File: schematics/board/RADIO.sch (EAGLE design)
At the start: 50 parts, among them J1 IPX-RADIO, J2 IPX-ANT

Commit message: Платки там
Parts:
- removed C1: 100nF, rcl:C-EUC0603
- removed C2: 220uF, UNKNOWN-2024:ECAPECAP220
- removed J1: IPX-RADIO, UNKNOWN-2024:U.FL-R-SMT-1_10_
- removed J2: IPX-ANT, UNKNOWN-2024:U.FL-R-SMT-1_10_
- removed LED1: AMP1, led:LEDCHIPLED_0603
- removed LED2: AMP2, led:LEDCHIPLED_0603
- removed NRF24LO1: NRF24L01_ML01SP4, UNKNOWN-2024:NRF24L01_ML01SP4
- removed R1, R2, R3, R4: 2k, rcl:R-US_R0603
- removed ROTATE1, ROTATE2, SW: CONNECT_3, UNKNOWN-2024:CONNECT_3
- removed XQ-02A: XQ-02A, UNKNOWN-2024:XQ-02A
- added JP1: (no value), pinhead:PINHD-1X10
- added JP2: (no value), pinhead:PINHD-1X16
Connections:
- removed net ANT_RADIO: J2.3, XQ-02A.ANT
- removed net N$1: LED1.C, R1.2
- removed net N$2: LED2.C, R2.2
- removed net N$3: LED1.A, ROTATE1.PIN
- removed net N$4: LED2.A, ROTATE2.PIN
- removed net N$5: R2.1, XQ-02A.LED2
- removed net N$6: R1.1, XQ-02A.LED1
- removed net N$7: R3.2, SW.P$1
- removed net N$8: R4.2, SW.P$3
- removed net RF-IN: J1.3, XQ-02A.RF-IN
- removed net SW: SW.PIN, XQ-02A.SW
- net 3V3: no longer NRF24LO1.VCC, ROTATE1.P$1, ROTATE2.P$1
- net 5V: no longer C1.2, C2.1, R3.1, XQ-02A.5V
- net CE_RADIO: no longer NRF24LO1.CE
- net CS_RADIO: no longer NRF24LO1.CSN
- net GND: no longer C1.1, C2.2, J1.1, J1.2, J2.1, J2.2, NRF24LO1.GND, R4.1, ROTATE1.P$3, ROTATE2.P$3, XQ-02A.GND
- net IRQ_RADIO: no longer NRF24LO1.IRQ
- net MISO_RADIO: no longer NRF24LO1.MISO
- net MOSI_RADIO: no longer NRF24LO1.MOSI
- net SCK_RADIO: no longer NRF24LO1.SCK

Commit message: ПЛАТЫ, АААААААААААААААААААААААААААА
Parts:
- added JP3: (no value), pinhead:PINHD-1X18
- added R1: 10k, rcl:R-US_R0603
- added R2: 100R, rcl:R-US_R0603
- added S1: (no value), UNKNOWN-2024:UNICS-SWITCHSS_12D11
- added SI2302CDS: SI2302CDS, CanCubeSat:SI2302CDS
- added U$10: LIS3MDL, UNKNOWN-2024:LIS3MDL
- added U$18: MOLEX-2-1.25, UNKNOWN-2024:MOLEX-2-1.25
- added U$4: E220-400T22S, UNKNOWN-2024:E220-400T22S
- added U$9: LSM6DS3_WITHOUT, UNKNOWN-2024:LSM6DS3_WITHOUT
- added X2: AKKUM, UNKNOWN-2024:JST-2-2.5
- JP2: device pinhead:PINHD-1X16 -> pinhead:PINHD-1X8
- U$6: value PBS_SMD_X13 -> MOLEX-2-1.25; device UNKNOWN-2024:PBS_SMD_X13 -> UNKNOWN-2024:MOLEX-2-1.25
- U$7: value PBS_SMD_X9 -> MOLEX-2-1.25; device UNKNOWN-2024:PBS_SMD_X9 -> UNKNOWN-2024:MOLEX-2-1.25
- U$8: value PBS_SMD_X13 -> JST-6-2.5; device UNKNOWN-2024:PBS_SMD_X13 -> UNKNOWN-2024:JST-6-2.5
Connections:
- removed net ADC_FOTO: U$6.10, U$8.4
- removed net CE_RADIO: U$7.1
- removed net CS_RADIO: U$7.2
- removed net DIR_DRIVER: U$6.2, U$8.12
- removed net IRQ_RADIO: U$7.3
- removed net LATCH_SR: U$6.5, U$8.9
- removed net MISO_RADIO: U$7.5
- removed net MOSI_RADIO: U$7.4
- removed net OE_SR: U$6.6, U$8.8
- removed net RX1_BLE: U$6.4, U$8.10
- removed net RX2_GPS: GPS-NEO7M.TX, U$7.8
- removed net SCK_RADIO: U$7.6
- removed net STEP_DRIVER: U$6.1, U$8.13
- removed net TX1_BLE: U$6.3, U$8.11
- removed net TX2_GPS: GPS-NEO7M.RX, U$7.7
- new net 3V7: JP1.10
- new net AUX_RADIO: JP3.10, U$4.AUX
- new net BUS+_OUT: S1.S, X2.1
- new net C0: JP2.1, JP3.1
- new net CS_LIS: JP1.8, U$10.CS
- new net CS_LSM: JP1.9, U$9.CS
- new net GERMO: JP3.18, R2.1
- new net LATCH: JP1.5, U$8.1
- new net M0_RADIO: JP3.12, U$4.M0
- new net M1_RADIO: JP3.11, U$4.M1
- new net MICS: JP2.4, JP3.4
- new net MISO_SENS: JP1.2
- new net MOSI: U$8.3
- new net MOSI_SENS: JP1.1
- new net N$2: R1.1, R2.2, SI2302CDS.G
- new net N$5: SI2302CDS.D, U$18.1, U$6.1, U$7.1
- new net NH3: JP2.3, JP3.3
- new net NO2: JP2.2, JP3.2
- new net OE: JP1.4, U$8.P$1
- new net RX_GPS: GPS-NEO7M.TX, JP3.14
- new net RX_LIDAR: JP3.15
- new net RX_RADIO: JP1.6, U$4.TXD
- new net SCK: U$8.2
- new net SCK_SENS: JP1.3
- new net SCL: JP2.8, JP3.9
- new net SDA: JP2.7, JP3.8
- new net SHIFT2: U$8.P$2
- new net SHIFT_2: JP3.17
- new net TX_GPS: GPS-NEO7M.RX, JP3.13
- new net TX_LIDAR: JP3.16
- new net TX_RADIO: JP1.7, U$4.RXD
- net 3V3: now also JP3.6, U$10.UCC, U$4.VCC, U$8.4, U$9.3V3; no longer U$6.13, U$8.1
- net 5V: now also JP2.6, JP3.7, U$18.2, U$6.2, U$7.2; no longer U$6.11, U$8.3
- net BUS+: now also S1.P
- net GND: now also JP2.5, JP3.5, R1.2, SI2302CDS.S, U$10.GND, U$4.GND, U$9.GND, X2.2; no longer U$6.12, U$8.2
- net MISO_SR: now also U$10.SDO, U$9.CAO; no longer U$6.8, U$8.6
- net MOSI_SR: now also U$10.SDA, U$9.SDA; no longer U$6.9, U$8.5
- net SCK_SR: now also U$10.SCL, U$9.SCL; no longer U$6.7, U$8.7
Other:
- moved on the sheet: 3V3, 5V, C10, C11, C12, C13, C14, C15, C16, C3, C4, C5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

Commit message: схемы плат
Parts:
- removed U$18, U$6, U$7: MOLEX-2-1.25, UNKNOWN-2024:MOLEX-2-1.25
- added COMPRESS, VALVE1, VALVE2: MOLEX-2-1.25, UNKNOWN-2024:MOLEX-2-1.25
- LSM6DS3: value LSM6DS3_WITHOUT -> LSM6DS3
- renumbered U$4 to RADIO, U$9 to LSM6DS3
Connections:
- net 5V: now also COMPRESS.2, VALVE1.2, VALVE2.2; no longer U$18.2, U$6.2, U$7.2
- net N$5: now also COMPRESS.1, VALVE1.1, VALVE2.1; no longer U$18.1, U$6.1, U$7.1
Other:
- moved on the sheet: 3V3, 5V, C10, C11, C12, C13, C14, C15, C16, C3, C4, C5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

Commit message: подготовлены файлы для зимней сессии
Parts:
- X2: device UNKNOWN-2024:JST-2-2.5 -> UNKNOWN-2024:JST-3-2.5
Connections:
- net LATCH renamed LATCH_SR
- net OE renamed OE_SR
- removed net 3V7: JP1.10
- removed net MISO_SR: LSM6DS3.CAO, U$10.SDO
- removed net MOSI: U$8.3
- removed net MOSI_SR: LSM6DS3.SDA, U$10.SDA
- removed net SCK: U$8.2
- removed net SCK_SR: LSM6DS3.SCL, U$10.SCL
- removed net SHIFT2: U$8.P$2
- removed net SHIFT_2: JP3.17
- new net 4V: JP1.10, X2.3
- new net SHIFT: JP3.17, U$8.P$2
- net MISO_SENS: now also LSM6DS3.CAO, U$10.SDO
- net MOSI_SENS: now also LSM6DS3.SDA, U$10.SDA, U$8.3
- net SCK_SENS: now also LSM6DS3.SCL, U$10.SCL, U$8.2
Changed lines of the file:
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@@
 <part name="U$10" library="UNKNOWN-2024" deviceset="LIS3MDL" device=""/>
 <part name="S1" library="UNKNOWN-2024" deviceset="UNICS-SWITCH" device="SS_12D11"/>
-<part name="X2" library="UNKNOWN-2024" deviceset="JST-2-2.5" device="" value="AKKUM"/>
+<part name="X2" library="UNKNOWN-2024" deviceset="JST-3-2.5" device="" value="AKKUM"/>
 <part name="JP2" library="pinhead" library_urn="urn:adsk.eagle:library:325" deviceset="PINHD-1X8" device="" package3d_urn="urn:adsk.eagle:package:22409/2"/>
 <part name="SI2302CDS" library="CanCubeSat" deviceset="SI2302CDS" device=""/>
@@
 <sheet>
 <plain>
+<wire x1="-76.2" y1="175.26" x2="304.8" y2="175.26" width="0.1524" layer="90"/>
+<wire x1="304.8" y1="175.26" x2="304.8" y2="-27.94" width="0.1524" layer="90"/>
+<wire x1="304.8" y1="-27.94" x2="-76.2" y2="-27.94" width="0.1524" layer="90"/>
+<wire x1="-76.2" y1="-27.94" x2="-76.2" y2="175.26" width="0.1524" layer="90"/>
 </plain>
 <instances>
@@
 <instance part="X2" gate="G$1" x="-15.24" y="127" smashed="yes">
 <attribute name="VALUE" x="-16.51" y="119.38" size="1.778" layer="96"/>
-<attribute name="NAME" x="-16.51" y="130.302" size="1.778" layer="95"/>
+<attribute name="NAME" x="-16.51" y="132.842" size="1.778" layer="95"/>
 </instance>
 <instance part="JP2" gate="A" x="-45.72" y="25.4" smashed="yes">
@@
 <pinref part="LSM6DS3" gate="G$1" pin="GND"/>
 <wire x1="48.26" y1="99.06" x2="58.42" y2="99.06" width="0.1524" layer="91"/>
-<label x="55.88" y="99.06" size="1.778" layer="95"/>
+<label x="53.34" y="99.06" size="1.778" layer="95"/>
 </segment>
 <segment>
 <pinref part="U$10" gate="G$1" pin="GND"/>
-<wire x1="38.1" y1="53.34" x2="25.4" y2="53.34" width="0.1524" layer="91"/>
-<label x="25.4" y="53.34" size="1.778" layer="95"/>
+<wire x1="38.1" y1="53.34" x2="22.86" y2="53.34" width="0.1524" layer="91"/>
+<label x="22.86" y="53.34" size="1.778" layer="95"/>
 </segment>
 <segment>
@@
 <pinref part="LSM6DS3" gate="G$1" pin="3V3"/>
 <wire x1="48.26" y1="104.14" x2="63.5" y2="104.14" width="0.1524" layer="91"/>
-<label x="55.88" y="104.14" size="1.778" layer="95"/>
+<label x="53.34" y="104.14" size="1.778" layer="95"/>
 </segment>
 <segment>
 <pinref part="U$10" gate="G$1" pin="UCC"/>
-<wire x1="38.1" y1="58.42" x2="25.4" y2="58.42" width="0.1524" layer="91"/>
-<label x="25.4" y="58.42" size="1.778" layer="95"/>
+<wire x1="38.1" y1="58.42" x2="22.86" y2="58.42" width="0.1524" layer="91"/>
+<label x="22.86" y="58.42" size="1.778" layer="95"/>
 </segment>
 <segment>
@@
 </segment>
 </net>
-<net name="SCK_SR" class="0">
-<segment>
-<pinref part="LSM6DS3" gate="G$1" pin="SCL"/>
-<wire x1="48.26" y1="93.98" x2="63.5" y2="93.98" width="0.1524" layer="91"/>
-<label x="55.88" y="93.98" size="1.778" layer="95"/>
-</segment>
-<segment>
-<pinref part="U$10" gate="G$1" pin="SCL"/>
-<wire x1="38.1" y1="48.26" x2="25.4" y2="48.26" width="0.1524" layer="91"/>
-<label x="25.4" y="48.26" size="1.778" layer="95"/>
-</segment>
-</net>
-<net name="MISO_SR" class="0">
-<segment>
-<pinref part="U$10" gate="G$1" pin="SDO"/>
-<wire x1="38.1" y1="38.1" x2="25.4" y2="38.1" width="0.1524" layer="91"/>
-<label x="25.4" y="38.1" size="1.778" layer="95"/>
-</segment>
-<segment>
-<pinref part="LSM6DS3" gate="G$1" pin="CAO"/>
-<wire x1="48.26" y1="78.74" x2="63.5" y2="78.74" width="0.1524" layer="91"/>
-<label x="55.88" y="78.74" size="1.778" layer="95"/>
-</segment>
-</net>
-<net name="MOSI_SR" class="0">
-<segment>
-<pinref part="LSM6DS3" gate="G$1" pin="SDA"/>
-<wire x1="48.26" y1="88.9" x2="63.5" y2="88.9" width="0.1524" layer="91"/>
-<label x="55.88" y="88.9" size="1.778" layer="95"/>
-</segment>
-<segment>
-<pinref part="U$10" gate="G$1" pin="SDA"/>
-<wire x1="38.1" y1="43.18" x2="25.4" y2="43.18" width="0.1524" layer="91"/>
-<label x="25.4" y="43.18" size="1.778" layer="95"/>
-</segment>
-</net>
 <net name="BUS+" class="0">
 <segment>
@@
 <pinref part="LSM6DS3" gate="G$1" pin="CS"/>
 <wire x1="48.26" y1="83.82" x2="63.5" y2="83.82" width="0.1524" layer="91"/>
-<label x="55.88" y="83.82" size="1.778" layer="95"/>
+<label x="53.34" y="83.82" size="1.778" layer="95"/>
 </segment>
 <segment>
@@
 <segment>
 <pinref part="U$10" gate="G$1" pin="CS"/>
-<wire x1="38.1" y1="33.02" x2="25.4" y2="33.02" width="0.1524" layer="91"/>
-<label x="25.4" y="33.02" size="1.778" layer="95"/>
+<wire x1="38.1" y1="33.02" x2="22.86" y2="33.02" width="0.1524" layer="91"/>
+<label x="22.86" y="33.02" size="1.778" layer="95"/>
 </segment>
 <segment>
@@
 <pinref part="JP1" gate="A" pin="1"/>
 </segment>
+<segment>
+<pinref part="LSM6DS3" gate="G$1" pin="SDA"/>
+<wire x1="48.26" y1="88.9" x2="63.5" y2="88.9" width="0.1524" layer="91"/>
+<label x="53.34" y="88.9" size="1.778" layer="95"/>
+</segment>
+<segment>
+<pinref part="U$10" gate="G$1" pin="SDA"/>
+<wire x1="38.1" y1="43.18" x2="22.86" y2="43.18" width="0.1524" layer="91"/>
+<label x="22.86" y="43.18" size="1.778" layer="95"/>
+</segment>
+<segment>
+<pinref part="U$8" gate="G$1" pin="3"/>
+<wire x1="238.76" y1="71.12" x2="256.54" y2="71.12" width="0.1524" layer="91"/>
+<label x="248.92" y="71.12" size="1.778" layer="95"/>
+</segment>
 </net>
 <net name="MISO_SENS" class="0">
@@
 <pinref part="JP1" gate="A" pin="2"/>
 </segment>
+<segment>
+<pinref part="LSM6DS3" gate="G$1" pin="CAO"/>
+<wire x1="48.26" y1="78.74" x2="63.5" y2="78.74" width="0.1524" layer="91"/>
+<label x="53.34" y="78.74" size="1.778" layer="95"/>
+</segment>
+<segment>
+<pinref part="U$10" gate="G$1" pin="SDO"/>
+<wire x1="38.1" y1="38.1" x2="22.86" y2="38.1" width="0.1524" layer="91"/>
+<label x="22.86" y="38.1" size="1.778" layer="95"/>
+</segment>
 </net>
 <net name="SCK_SENS" class="0">
@@
 <pinref part="JP1" gate="A" pin="3"/>
 </segment>
-</net>
-<net name="OE" class="0">
-<segment>
-<wire x1="-48.26" y1="121.92" x2="-68.58" y2="121.92" width="0.1524" layer="91"/>
-<label x="-68.58" y="121.92" size="1.778" layer="95"/>
-<pinref part="JP1" gate="A" pin="4"/>
-</segment>
-<segment>
-<pinref part="U$8" gate="G$1" pin="P$1"/>
-<wire x1="238.76" y1="63.5" x2="256.54" y2="63.5" width="0.1524" layer="91"/>
-<label x="248.92" y="63.5" size="1.778" layer="95"/>
-</segment>
-</net>
-<net name="LATCH" class="0">
-<segment>
-<wire x1="-48.26" y1="119.38" x2="-68.58" y2="119.38" width="0.1524" layer="91"/>
-<label x="-68.58" y="119.38" size="1.778" layer="95"/>
-<pinref part="JP1" gate="A" pin="5"/>
-</segment>
-<segment>
-<pinref part="U$8" gate="G$1" pin="1"/>
-<wire x1="238.76" y1="66.04" x2="256.54" y2="66.04" width="0.1524" layer="91"/>
-<label x="248.92" y="66.04" size="1.778" layer="95"/>
-</segment>
-</net>
-<net name="3V7" class="0">
+<segment>
+<pinref part="LSM6DS3" gate="G$1" pin="SCL"/>
+<wire x1="48.26" y1="93.98" x2="63.5" y2="93.98" width="0.1524" layer="91"/>
+<label x="53.34" y="93.98" size="1.778" layer="95"/>
+</segment>
+<segment>
+<pinref part="U$10" gate="G$1" pin="SCL"/>
+<wire x1="38.1" y1="48.26" x2="22.86" y2="48.26" width="0.1524" layer="91"/>
+<label x="22.86" y="48.26" size="1.778" layer="95"/>
+</segment>
+<segment>
+<pinref part="U$8" gate="G$1" pin="2"/>
+<wire x1="238.76" y1="68.58" x2="256.54" y2="68.58" width="0.1524" layer="91"/>
+<label x="248.92" y="68.58" size="1.778" layer="95"/>
+</segment>
+</net>
+<net name="4V" class="0">
 <segment>
 <pinref part="JP1" gate="A" pin="10"/>
 <wire x1="-48.26" y1="106.68" x2="-68.58" y2="106.68" width="0.1524" layer="91"/>
 <label x="-68.58" y="106.68" size="1.778" layer="95"/>
+</segment>
+<segment>
+<pinref part="X2" gate="G$1" pin="3"/>
+<wire x1="-7.62" y1="129.54" x2="7.62" y2="129.54" width="0.1524" layer="91"/>
+<label x="-2.54" y="129.54" size="1.778" layer="95"/>
 </segment>
 </net>
@@
 </segment>
 </net>
-<net name="SHIFT_2" class="0">
+<net name="SHIFT" class="0">
 <segment>
 <wire x1="-68.58" y1="50.8" x2="-48.26" y2="50.8" width="0.1524" layer="91"/>
@@
 <pinref part="JP3" gate="A" pin="17"/>
 </segment>
+<segment>
+<pinref part="U$8" gate="G$1" pin="P$2"/>
+<wire x1="238.76" y1="60.96" x2="256.54" y2="60.96" width="0.1524" layer="91"/>
+<label x="248.92" y="60.96" size="1.778" layer="95"/>
+</segment>
 </net>
 <net name="RX_LIDAR" class="0">
@@
 </segment>
 </net>
-<net name="MOSI" class="0">
-<segment>
-<pinref part="U$8" gate="G$1" pin="3"/>
-<wire x1="238.76" y1="71.12" x2="256.54" y2="71.12" width="0.1524" layer="91"/>
-<label x="248.92" y="71.12" size="1.778" layer="95"/>
-</segment>
-</net>
-<net name="SCK" class="0">
-<segment>
-<pinref part="U$8" gate="G$1" pin="2"/>
-<wire x1="238.76" y1="68.58" x2="256.54" y2="68.58" width="0.1524" layer="91"/>
-<label x="248.92" y="68.58" size="1.778" layer="95"/>
-</segment>
-</net>
-<net name="SHIFT2" class="0">
-<segment>
-<pinref part="U$8" gate="G$1" pin="P$2"/>
-<wire x1="238.76" y1="60.96" x2="256.54" y2="60.96" width="0.1524" layer="91"/>
-<label x="248.92" y="60.96" size="1.778" layer="95"/>
-</segment>
-</net>
+<net name="OE_SR" class="0">
+<segment>
+<wire x1="-48.26" y1="121.92" x2="-68.58" y2="121.92" width="0.1524" layer="91"/>
+<label x="-68.58" y="121.92" size="1.778" layer="95"/>
+<pinref part="JP1" gate="A" pin="4"/>
+</segment>
+<segment>
+<pinref part="U$8" gate="G$1" pin="P$1"/>
+<wire x1="238.76" y1="63.5" x2="256.54" y2="63.5" width="0.1524" layer="91"/>
+<label x="248.92" y="63.5" size="1.778" layer="95"/>
+</segment>
+</net>
+<net name="LATCH_SR" class="0">
+<segment>
+<wire x1="-48.26" y1="119.38" x2="-68.58" y2="119.38" width="0.1524" layer="91"/>
+<label x="-68.58" y="119.38" size="1.778" layer="95"/>
+<pinref part="JP1" gate="A" pin="5"/>
+</segment>
+<segment>
+<pinref part="U$8" gate="G$1" pin="1"/>
+<wire x1="238.76" y1="66.04" x2="256.54" y2="66.04" width="0.1524" layer="91"/>
+<label x="248.92" y="66.04" size="1.778" layer="95"/>
+</segment>
+</net>

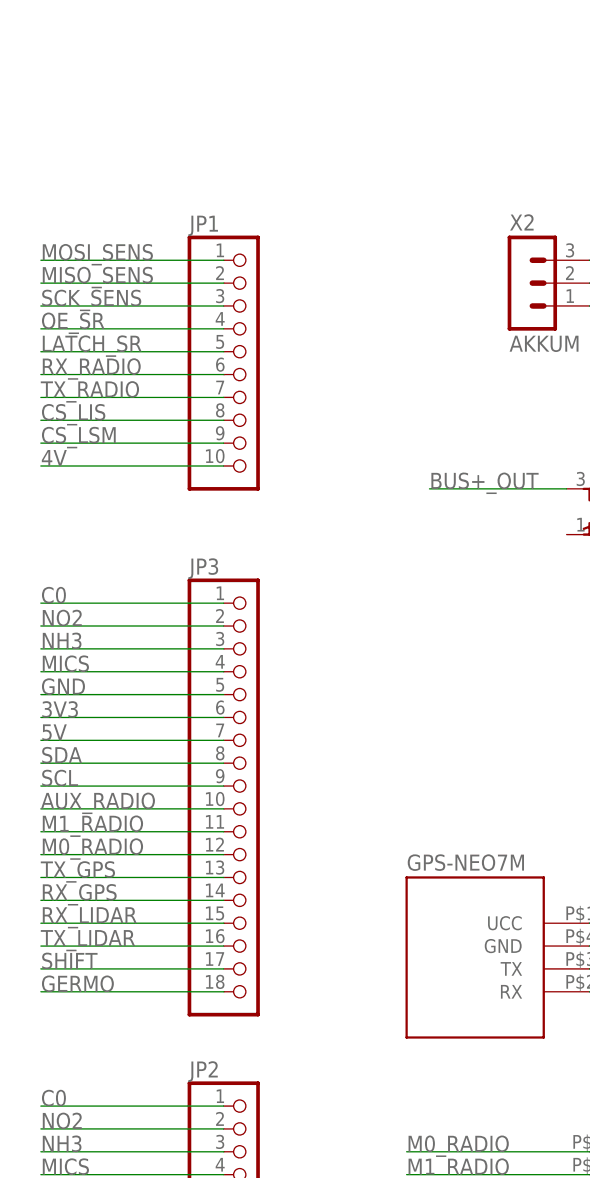
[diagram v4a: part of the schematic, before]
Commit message: распиновка разъемов плат
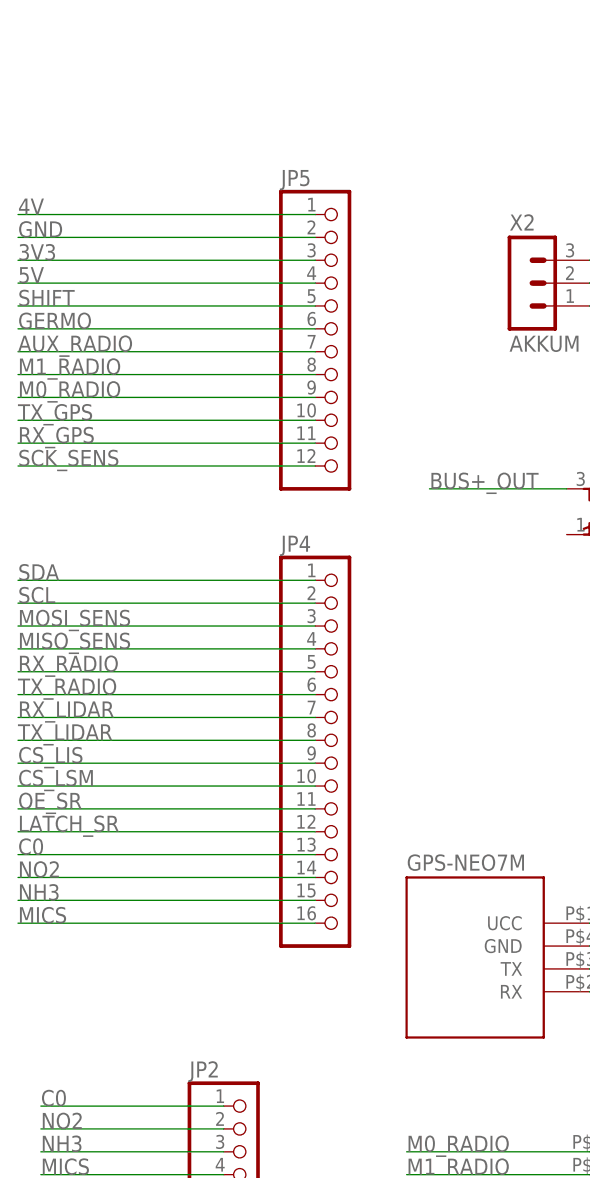
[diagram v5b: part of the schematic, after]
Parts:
- removed JP1: (no value), pinhead:PINHD-1X10
- removed JP3: (no value), pinhead:PINHD-1X18
- added JP4: (no value), pinhead:PINHD-1X16
- added JP5: (no value), pinhead:PINHD-1X12
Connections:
- net 3V3: now also JP5.3; no longer JP3.6
- net 4V: now also JP5.1; no longer JP1.10
- net 5V: now also JP5.4; no longer JP3.7
- net AUX_RADIO: now also JP5.7; no longer JP3.10
- net C0: now also JP4.13; no longer JP3.1
- net CS_LIS: now also JP4.9; no longer JP1.8
- net CS_LSM: now also JP4.10; no longer JP1.9
- net GERMO: now also JP5.6; no longer JP3.18
- net GND: now also JP5.2; no longer JP3.5
- net LATCH_SR: now also JP4.12; no longer JP1.5
- net M0_RADIO: now also JP5.9; no longer JP3.12
- net M1_RADIO: now also JP5.8; no longer JP3.11
- net MICS: now also JP4.16; no longer JP3.4
- net MISO_SENS: now also JP4.4; no longer JP1.2
- net MOSI_SENS: now also JP4.3; no longer JP1.1
- net NH3: now also JP4.15; no longer JP3.3
- net NO2: now also JP4.14; no longer JP3.2
- net OE_SR: now also JP4.11; no longer JP1.4
- net RX_GPS: now also JP5.11; no longer JP3.14
- net RX_LIDAR: now also JP4.7; no longer JP3.15
- net RX_RADIO: now also JP4.5; no longer JP1.6
- net SCK_SENS: now also JP5.12; no longer JP1.3
- net SCL: now also JP4.2; no longer JP3.9
- net SDA: now also JP4.1; no longer JP3.8
- net SHIFT: now also JP5.5; no longer JP3.17
- net TX_GPS: now also JP5.10; no longer JP3.13
- net TX_LIDAR: now also JP4.8; no longer JP3.16
- net TX_RADIO: now also JP4.6; no longer JP1.7

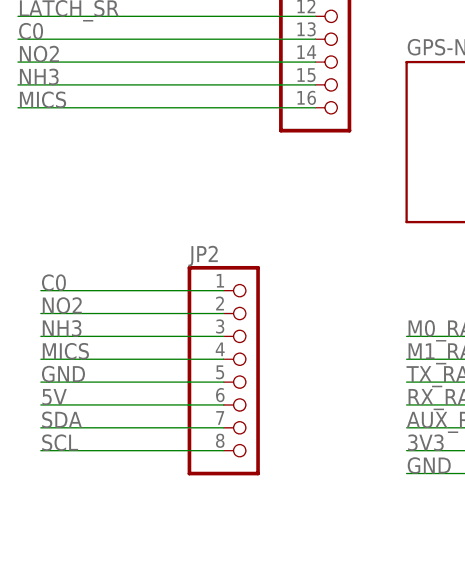
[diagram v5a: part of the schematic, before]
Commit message: разъем в гермообъеме на 8 пинов
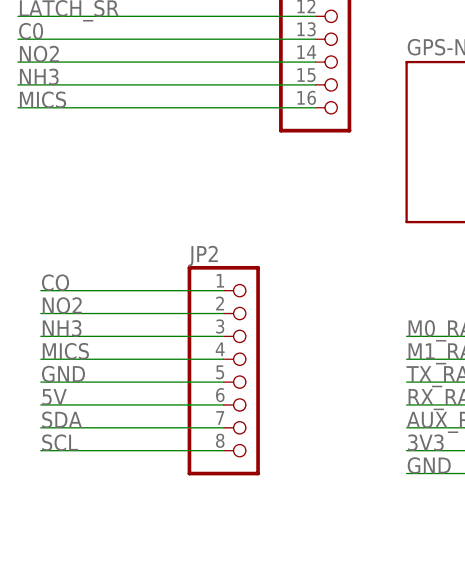
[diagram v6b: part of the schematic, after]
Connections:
- new net CO: JP2.1
- net C0: no longer JP2.1
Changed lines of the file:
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@@
 <net name="C0" class="0">
-<segment>
-<wire x1="-48.26" y1="35.56" x2="-68.58" y2="35.56" width="0.1524" layer="91"/>
-<label x="-68.58" y="35.56" size="1.778" layer="95"/>
-<pinref part="JP2" gate="A" pin="1"/>
-</segment>
 <segment>
 <wire x1="-38.1" y1="63.5" x2="-71.12" y2="63.5" width="0.1524" layer="91"/>
@@
 </segment>
 </net>
+<net name="CO" class="0">
+<segment>
+<wire x1="-48.26" y1="35.56" x2="-68.58" y2="35.56" width="0.1524" layer="91"/>
+<label x="-68.58" y="35.56" size="1.778" layer="95"/>
+<pinref part="JP2" gate="A" pin="1"/>
+</segment>
+</net>

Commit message: Плата Радио
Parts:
- removed JP2: (no value), pinhead:PINHD-1X8
- added JP1, JP3: (no value), pinhead:PINHD-1X4
- added U$7: MOLEX-4-1.25, UNKNOWN-2024:MOLEX-4-1.25
- U$8: value JST-6-2.5 -> MOLEX-5-1.25; device UNKNOWN-2024:JST-6-2.5 -> UNKNOWN-2024:MOLEX-5-1.25
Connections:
- net 3V3: now also U$8.5; no longer U$8.4
- net 5V: now also JP3.2, U$7.3; no longer JP2.6
- net CO: now also JP1.1; no longer JP2.1
- net GND: now also JP3.1, U$7.4; no longer JP2.5
- net LATCH_SR: now also U$8.3; no longer U$8.1
- net MICS: now also JP1.4; no longer JP2.4
- net MOSI_SENS: no longer U$8.3
- net NH3: now also JP1.3; no longer JP2.3
- net NO2: now also JP1.2; no longer JP2.2
- net OE_SR: now also U$8.2; no longer U$8.P$1
- net RX_LIDAR: now also U$7.2
- net SCK_SENS: now also U$8.4; no longer U$8.2
- net SCL: now also JP3.4; no longer JP2.8
- net SDA: now also JP3.3; no longer JP2.7
- net SHIFT: now also U$8.1; no longer U$8.P$2
- net TX_LIDAR: now also U$7.1
